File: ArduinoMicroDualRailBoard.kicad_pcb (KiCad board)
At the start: 2 copper layers, 135.3 x 92.7 mm, 58 parts, among them J1 Conn_01x20_Male, J10 Conn_01x02_Male, J2 Screw_Terminal_01x03, J3 Conn_01x20_Male, J4 Conn_01x20_Male, J5 Screw_Terminal_01x03, J6 Conn_01x20_Male, J7 SDS-50J, J8 SDS-50J, J9 Screw_Terminal_01x03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

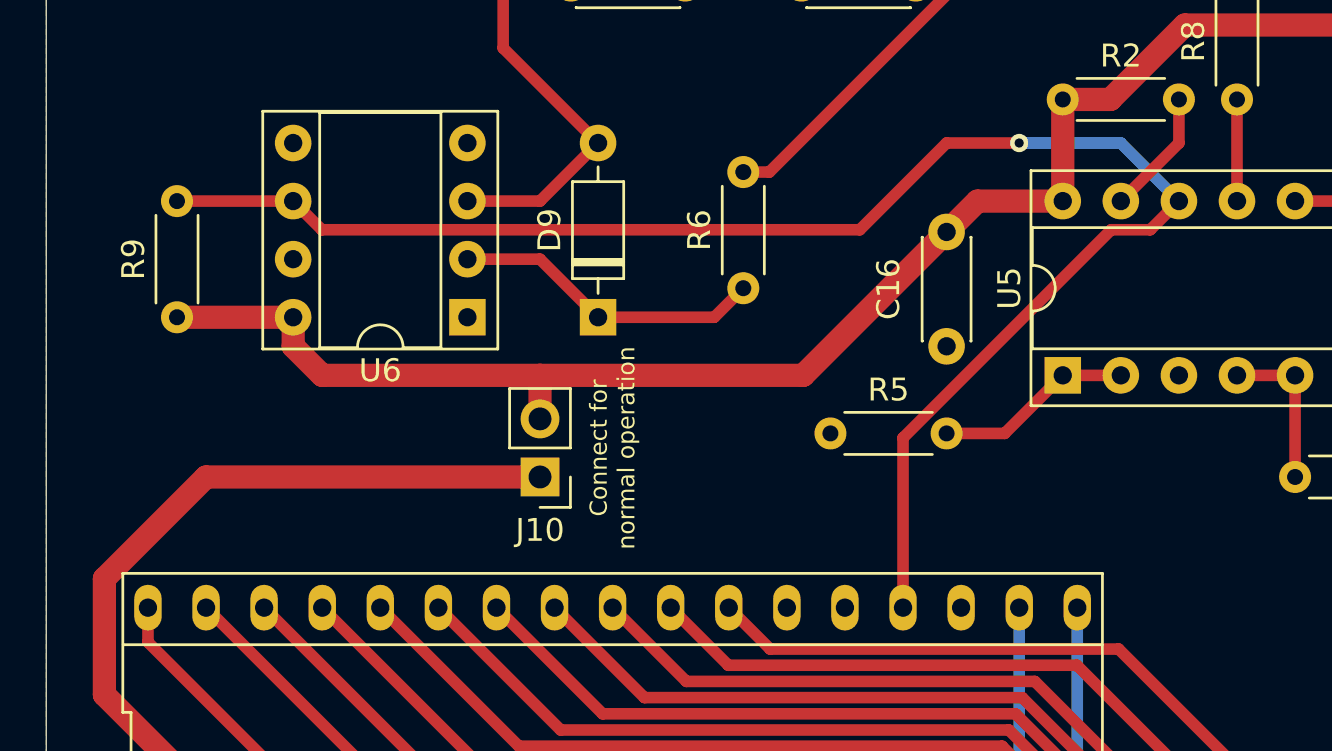
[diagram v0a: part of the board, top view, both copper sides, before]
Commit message: Added bypass cap for 6N138
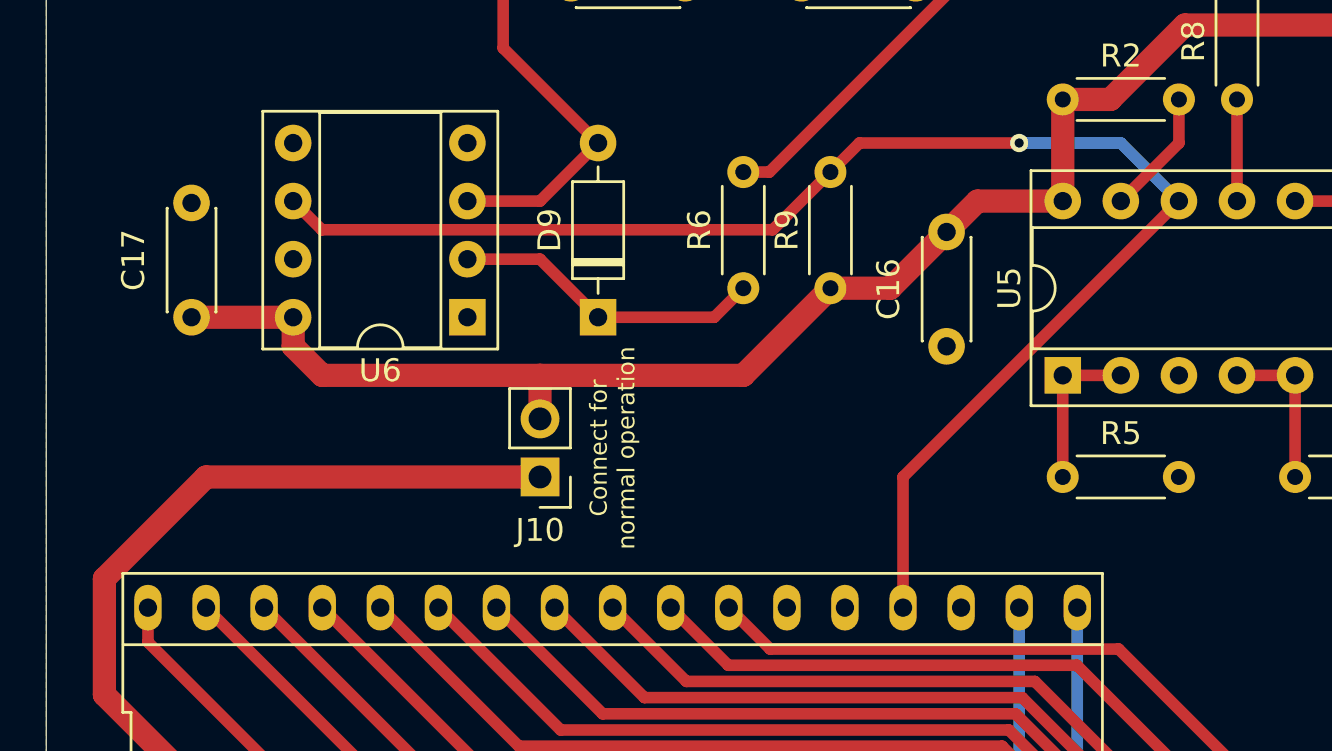
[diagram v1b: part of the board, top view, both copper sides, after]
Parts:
- added C17: 0.1uF, Capacitor_THT:C_Disc_D4.3mm_W1.9mm_P5.00mm, F.Cu at (90.8, 83.3)
- moved R9 28.6 mm to (118.7, 81.9)
- moved R5 5.43 mm to (128.9, 95.2), turned to 0 degrees
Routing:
- net /RX: track 70.7 -> 64.7 mm
- net Net-(R5-Pad1): track 8.67 -> 6.98 mm
- net +5V: track 186.0 -> 185.3 mm

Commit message: Regenerated gerbers, minor rerouting
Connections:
- J5 pad 1: -15V -> +15V
- J5 pad 3: +15V -> -15V
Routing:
- net -15V: track 77.8 -> 69.7 mm
- net +15V: track 95.5 -> 103.1 mm, vias 2 -> 0
